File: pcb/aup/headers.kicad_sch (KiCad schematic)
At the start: 4 parts, among them J1 DF40C-100DS-0.4V_51, J2 DF40C-100DS-0.4V_51, J3 DF40C-100DS-0.4V_51, J4 DF40C-100DS-0.4V_51

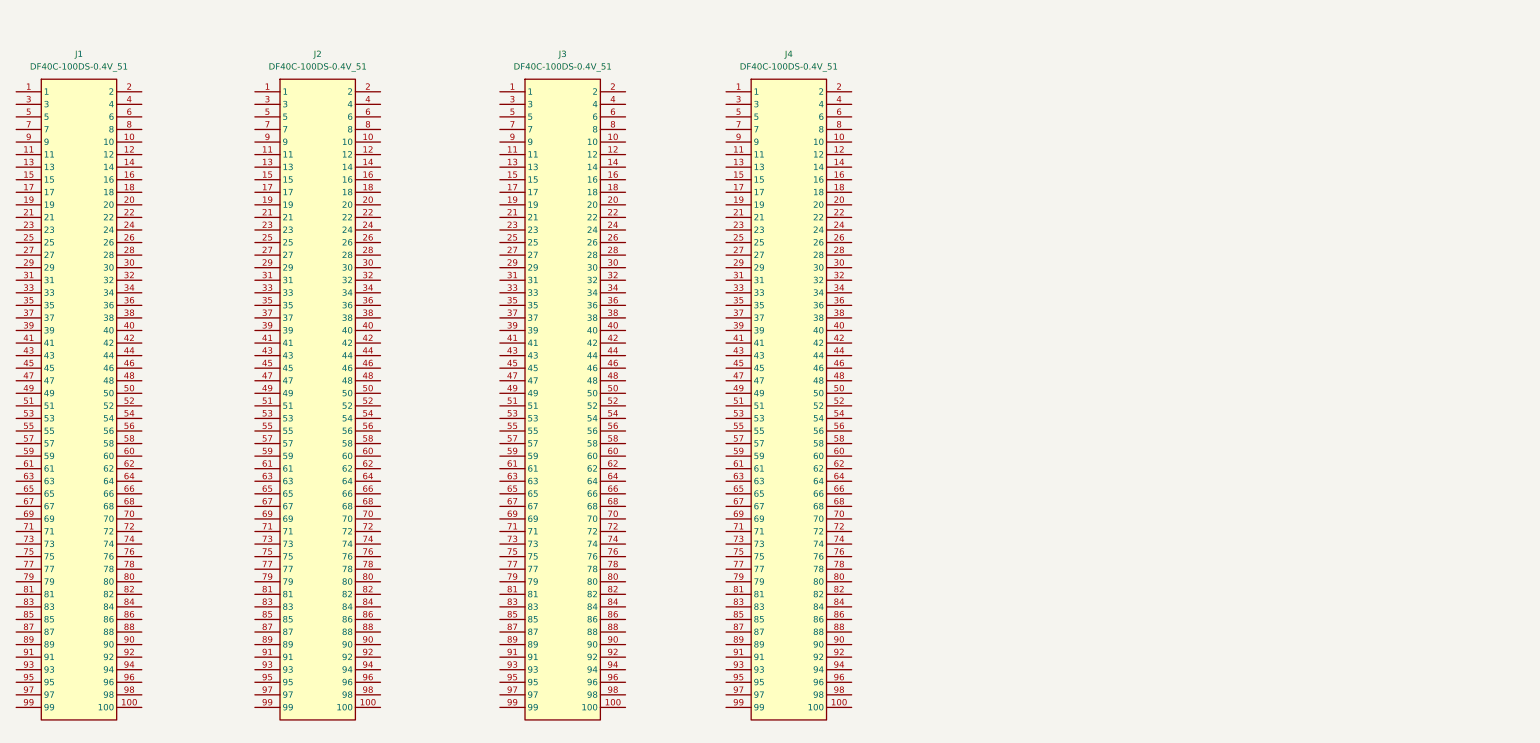
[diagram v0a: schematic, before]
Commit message: Switch to 50 pin sockets
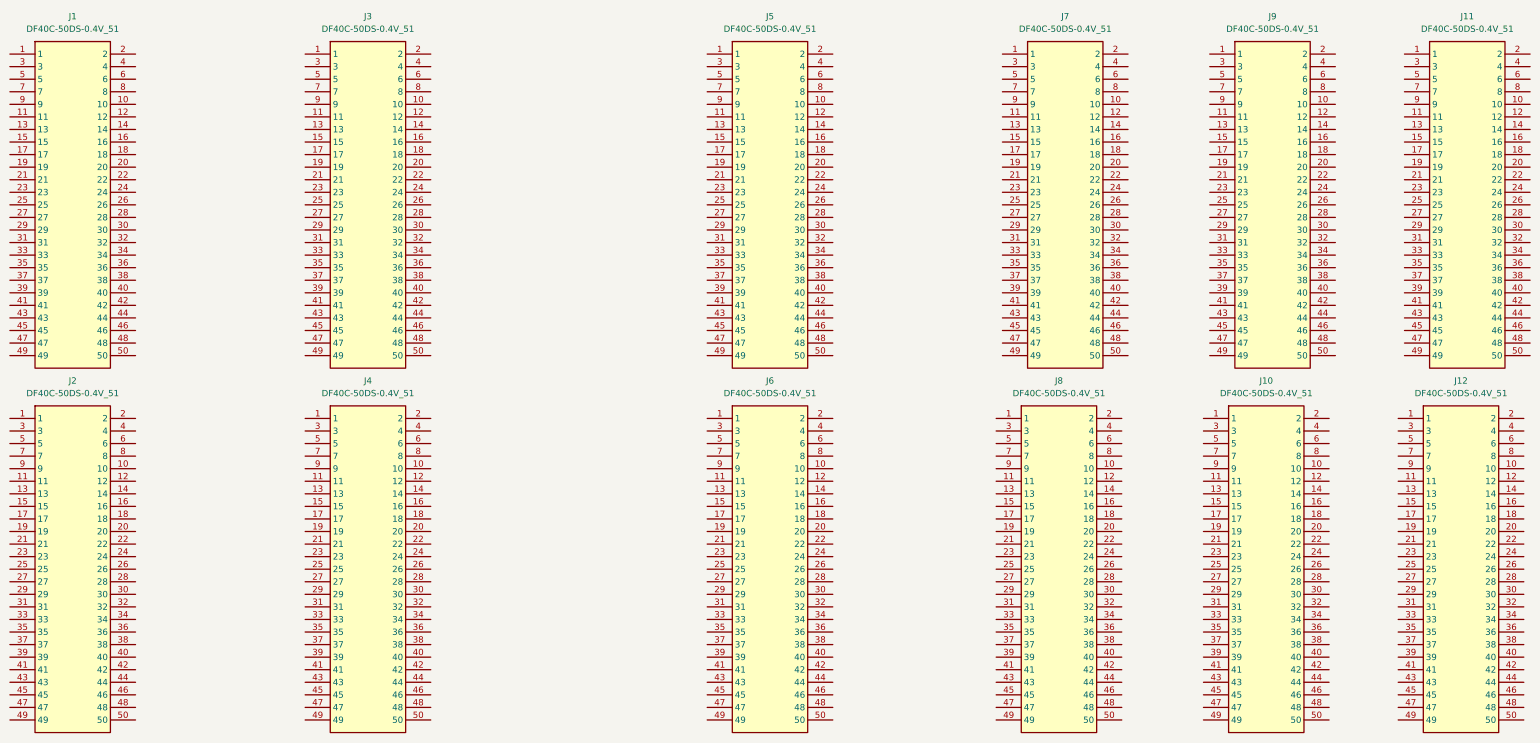
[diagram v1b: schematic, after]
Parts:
- removed J1, J2, J3, J4: DF40C-100DS-0.4V_51, !DF40C:DF40C100DS04V51, symbol !DF40C:DF40C-100DS-0.4V_51
- added J1, J10, J11, J12, J2, J3, J4, J5, J6, J7, J8, J9: DF40C-50DS-0.4V_51, !DF40C:DF40C50DS04VD1, symbol !DF40C:DF40C-50DS-0.4V_51

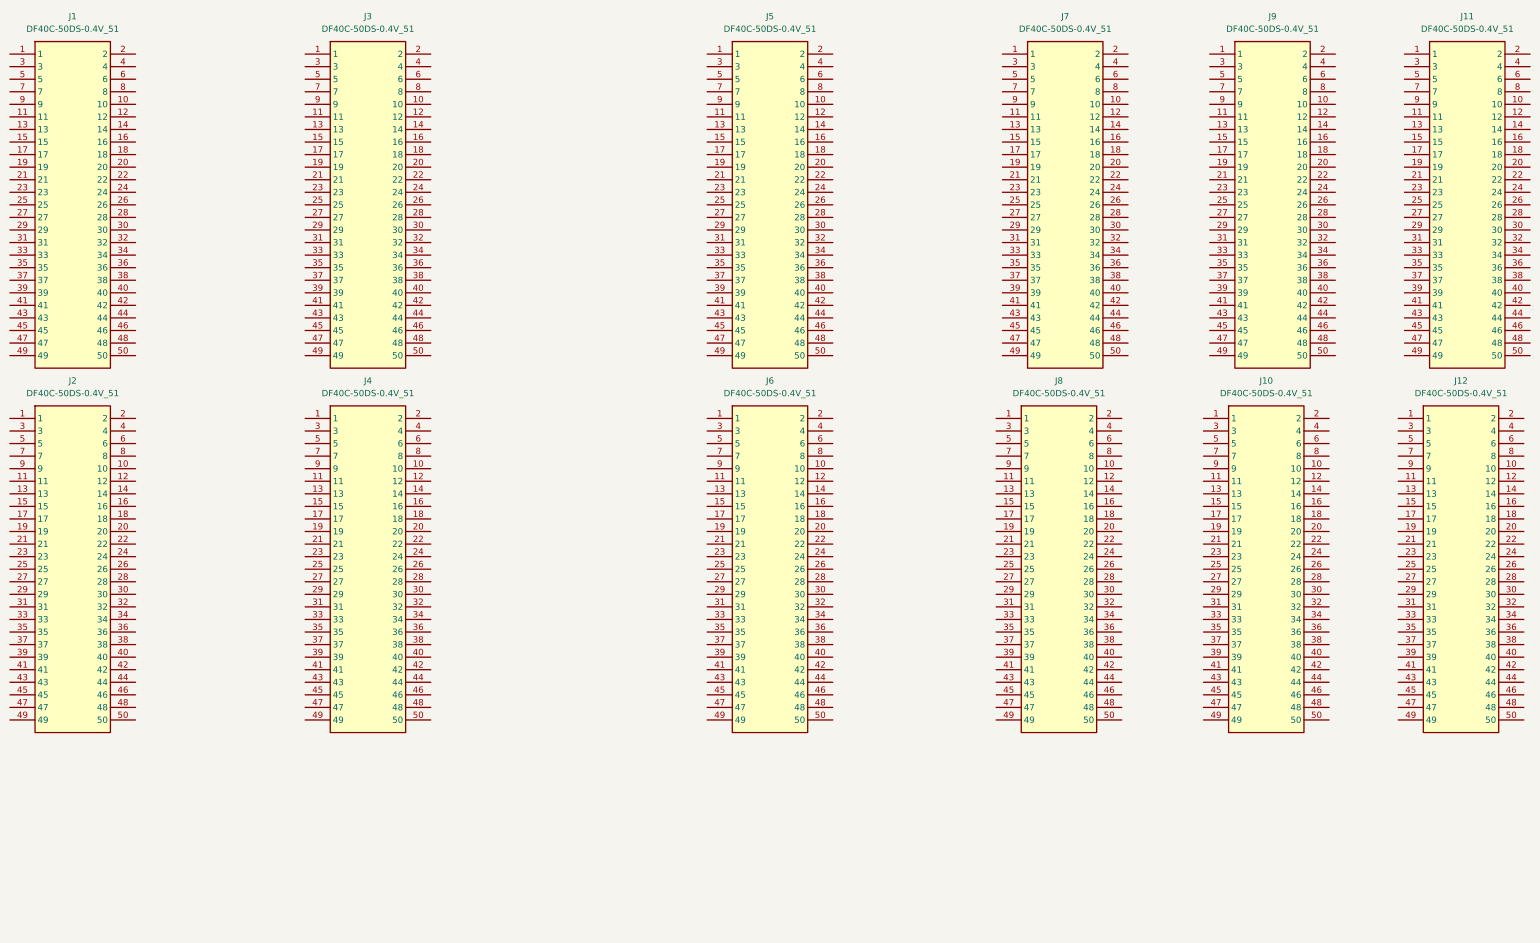
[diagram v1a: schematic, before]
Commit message: Switch to QSH-60
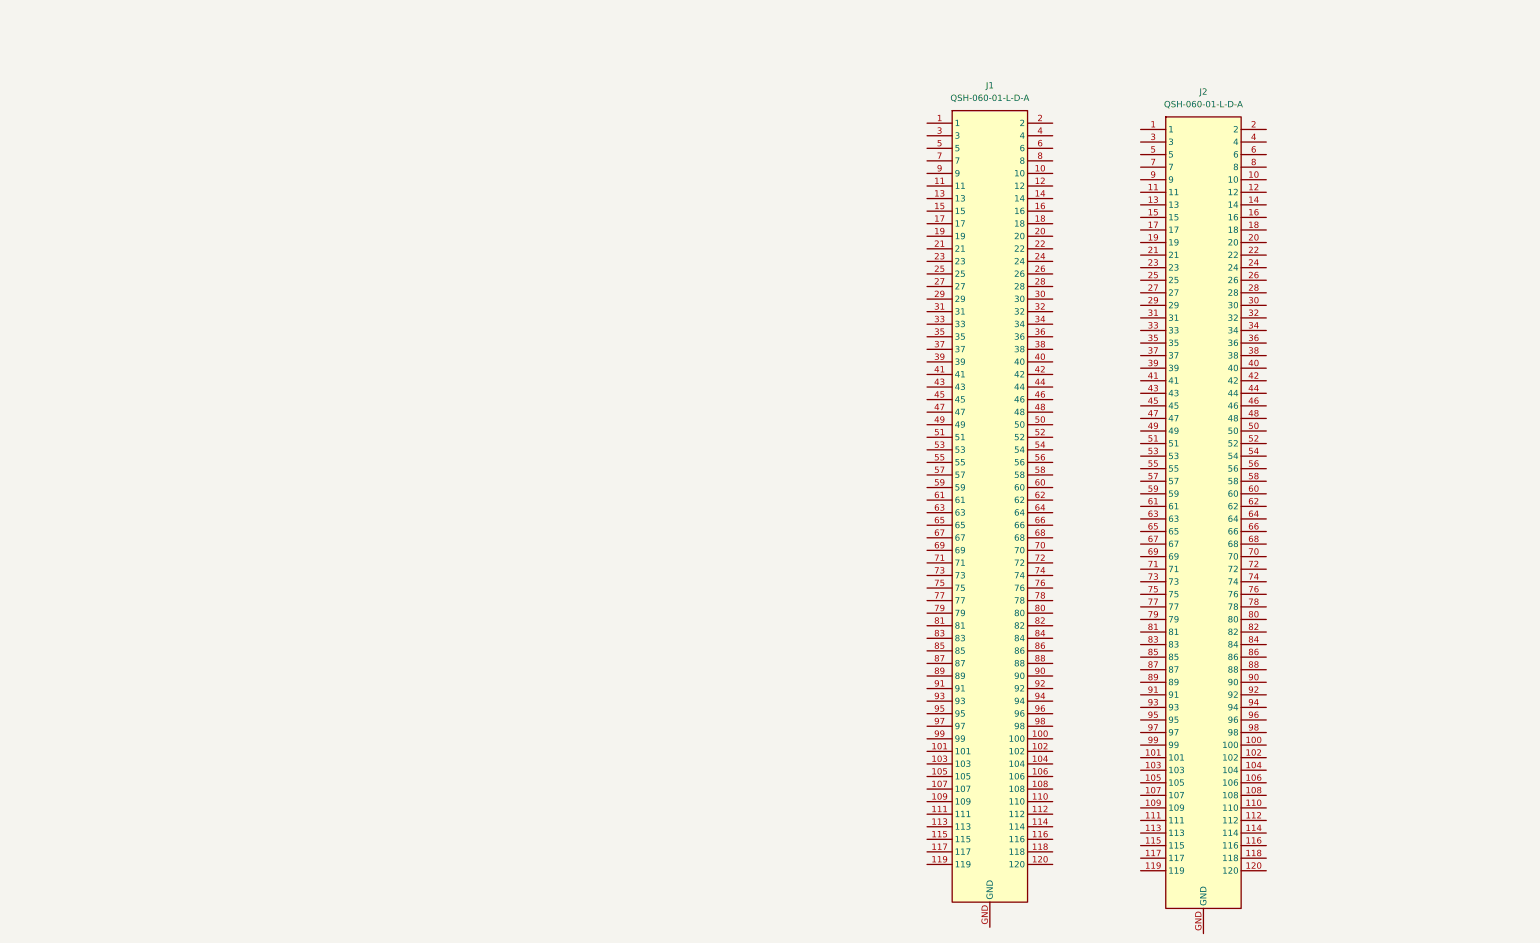
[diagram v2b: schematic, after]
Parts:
- removed J1, J10, J11, J12, J2, J3, J4, J5, J6, J7, J8, J9: DF40C-50DS-0.4V_51, !DF40C:DF40C50DS04VD1, symbol !DF40C:DF40C-50DS-0.4V_51
- added J1, J2: QSH-060-01-L-D-A, !Misc:SAMTEC_QSH-060-01-X-D-A, symbol !Misc:QSH-060-01-L-D-A

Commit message: Add upper connector
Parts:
- added J3, J4: QTH-060-01-L-D-A, !Misc:SAMTEC_QTH-060-01-X-D-A, symbol !Misc:QTH-060-01-L-D-A
- added J5: QSH-030-01-L-D-A, !Misc:SAMTEC_QSH-030-01-X-D-A, symbol !Misc:QSH-030-01-L-D-A
- added J6: QTH-030-01-L-D-A, !Misc:SAMTEC_QTH-030-01-X-D-A, symbol !Misc:QTH-030-01-L-D-A
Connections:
- net IOT_180: now reaches J1.1
- net IOT_180: now also J3.1
- net +3V3: now reaches J1.10
- net +3V3: now also J1.101, J1.102, J1.111, J1.112, J1.19, J1.20, J1.29, J1.30, J1.39, J1.40, J1.49, J1.50, J1.71, J1.72, J1.81, J1.82, J1.9, J1.91, J1.92, J2.10, J2.101, J2.102, J2.111, J2.112, J2.19, J2.20, J2.29, J2.30, J2.39, J2.40, J2.49, J2.50, J2.71, J2.72, J2.81, J2.82, J2.9, J2.91, J2.92, J3.10, J3.101, J3.102, J3.111, J3.112, J3.19, J3.20, J3.29, J3.30, J3.39, J3.40, J3.49, J3.50, J3.71, J3.72, J3.81, J3.82, J3.9, J3.91, J3.92, J4.10, J4.101, J4.102, J4.111, J4.112, J4.19, J4.20, J4.29, J4.30, J4.39, J4.40, J4.49, J4.50, J4.71, J4.72, J4.81, J4.82, J4.9, J4.91, J4.92
- net IOL_17B: now reaches J1.100
- net IOL_17B: now also J3.100
- net IOL_7A: now reaches J1.103
- net IOL_7A: now also J3.103
- net IOL_20B: now reaches J1.104
- net IOL_20B: now also J3.104
- net IOL_21A: now reaches J1.105
- net IOL_21A: now also J3.105
- net IOL_18B: now reaches J1.106
- net IOL_18B: now also J3.106
- net IOL_12A: now reaches J1.107
- net IOL_12A: now also J3.107
- net IOL_21B: now reaches J1.108
- net IOL_21B: now also J3.108
- net IOL_26B: now reaches J1.109
- net IOL_26B: now also J3.109
- net IOT_181: now reaches J1.11
- net IOT_181: now also J3.11
- net IOL_24A: now reaches J1.110
- net IOL_24A: now also J3.110
- net IOL_25B: now reaches J1.113
- net IOL_25B: now also J3.113
- net IOL_25A: now reaches J1.114
- net IOL_25A: now also J3.114
- net IOL_16B: now reaches J1.115
- net IOL_16B: now also J3.115
- net IOL_26A: now reaches J1.116
- net IOL_26A: now also J3.116
- net IOL_22A: now reaches J1.117
- net IOL_22A: now also J3.117
- net IOL_22B: now reaches J1.118
- net IOL_22B: now also J3.118
- net IOL_19B: now reaches J1.119
- net IOL_19B: now also J3.119
- net IOT_182: now reaches J1.12
- net IOT_182: now also J3.12
- net IOL_24B: now reaches J1.120
- net IOL_24B: now also J3.120
- net IOT_185: now reaches J1.13
- net IOT_185: now also J3.13
- net IOT_187: now reaches J1.14
- net IOT_187: now also J3.14
- net IOT_179: now reaches J1.15
- net IOT_179: now also J3.15
- net IOT_169: now reaches J1.16
- net IOT_169: now also J3.16
- net IOT_193: now reaches J1.17
- net IOT_193: now also J3.17
- net IOT_184: now reaches J1.18
- net IOT_184: now also J3.18
- net IOT_176: now reaches J1.2
- net IOT_176: now also J3.2
- net IOT_191: now reaches J1.21
- net IOT_191: now also J3.21
- net IOT_168: now reaches J1.22
- net IOT_168: now also J3.22
- net IOT_192: now reaches J1.23
- net IOT_192: now also J3.23
- net IOT_186: now reaches J1.24
- net IOT_186: now also J3.24
- net IOT_209: now reaches J1.25
- net IOT_209: now also J3.25
- net IOT_183: now reaches J1.26
- net IOT_183: now also J3.26
- net IOT_200: now reaches J1.27
- net IOT_200: now also J3.27
- net IOT_194: now reaches J1.28
- net IOT_194: now also J3.28
- net IOT_196: now reaches J1.3
- net IOT_196: now also J3.3
- net IOT_197: now reaches J1.31
- net IOT_197: now also J3.31
- net IOT_177: now reaches J1.32
- net IOT_177: now also J3.32
- net IOT_219: now reaches J1.33
- net IOT_219: now also J3.33
- net IOT_199: now reaches J1.34
- net IOT_199: now also J3.34
- net IOT_210: now reaches J1.35
- net IOT_210: now also J3.35
- net IOT_203: now reaches J1.36
- net IOT_203: now also J3.36
- net IOT_221: now reaches J1.37
- net IOT_221: now also J3.37
- net IOT_205: now reaches J1.38
- net IOT_205: now also J3.38
- net IOT_171: now reaches J1.4
- net IOT_171: now also J3.4
- net IOT_222: now reaches J1.41
- net IOT_222: now also J3.41
- net IOT_207: now reaches J1.42
- net IOT_207: now also J3.42
- net IOT_206: now reaches J1.43
- net IOT_206: now also J3.43
- net IOT_211: now reaches J1.44
- net IOT_211: now also J3.44
- net IOT_227: now reaches J1.45
- net IOT_227: now also J3.45
- net IOT_208: now reaches J1.46
- net IOT_208: now also J3.46
- net IOT_198: now reaches J1.47
- net IOT_198: now also J3.47
- net IOT_216: now reaches J1.48
- net IOT_216: now also J3.48
- net IOT_190: now reaches J1.5
- net IOT_190: now also J3.5
- net IOT_212: now reaches J1.51
- net IOT_212: now also J3.51
- net IOT_213: now reaches J1.52
- net IOT_213: now also J3.52
- net IOT_224: now reaches J1.53
- net IOT_224: now also J3.53
- net IOT_214: now reaches J1.54
- net IOT_214: now also J3.54
- net IOT_215: now reaches J1.55
- net IOT_215: now also J3.55
- net IOT_223: now reaches J1.56
- net IOT_223: now also J3.56
- net IOT_226: now reaches J1.57
- net IOT_226: now also J3.57
- net IOT_218: now reaches J1.58
- net IOT_218: now also J3.58
- net IOT_225: now reaches J1.59
- net IOT_225: now also J3.59
- net IOT_178: now reaches J1.6
- net IOT_178: now also J3.6
- net IOT_220: now reaches J1.60
- net IOT_220: now also J3.60
- net IOL_2A: now reaches J1.61
- net IOL_2A: now also J3.61
- net IOL_1B: now reaches J1.62
- net IOL_1B: now also J3.62
- net IOL_1A: now reaches J1.63
- net IOL_1A: now also J3.63
- net IOL_2B: now reaches J1.64
- net IOL_2B: now also J3.64
- net IOL_5A: now reaches J1.65
- net IOL_5A: now also J3.65
- net IOL_3B: now reaches J1.66
- net IOL_3B: now also J3.66
- net IOL_6B: now reaches J1.67
- net IOL_6B: now also J3.67
- net IOL_3A: now reaches J1.68
- net IOL_3A: now also J3.68
- net IOL_10A: now reaches J1.69
- net IOL_10A: now also J3.69
- net IOT_173: now reaches J1.7
- net IOT_173: now also J3.7
- net IOL_4B: now reaches J1.70
- net IOL_4B: now also J3.70
- net IOL_19A: now reaches J1.73
- net IOL_19A: now also J3.73
- net IOL_5B: now reaches J1.74
- net IOL_5B: now also J3.74
- net IOL_8B: now reaches J1.75
- net IOL_8B: now also J3.75
- net IOL_10B: now reaches J1.76
- net IOL_10B: now also J3.76
- net IOL_13A: now reaches J1.77
- net IOL_13A: now also J3.77
- net IOL_9B: now reaches J1.78
- net IOL_9B: now also J3.78
- net IOL_4A: now reaches J1.79
- net IOL_4A: now also J3.79
- net IOT_172: now reaches J1.8
- net IOT_172: now also J3.8
- net IOL_13B: now reaches J1.80
- net IOL_13B: now also J3.80
- net IOL_8A: now reaches J1.83
- net IOL_8A: now also J3.83
- net IOL_11B: now reaches J1.84
- net IOL_11B: now also J3.84
- net IOL_20A: now reaches J1.85
- net IOL_20A: now also J3.85
- net IOL_14B: now reaches J1.86
- net IOL_14B: now also J3.86
- net IOL_6A: now reaches J1.87
- net IOL_6A: now also J3.87
- net IOL_12B: now reaches J1.88
- net IOL_12B: now also J3.88
- net IOL_18A: now reaches J1.89
- net IOL_18A: now also J3.89
- net IOL_7B: now reaches J1.90
- net IOL_7B: now also J3.90
- net IOL_23A: now reaches J1.93
- net IOL_23A: now also J3.93
- net IOL_15B: now reaches J1.94
- net IOL_15B: now also J3.94
- net IOL_9A: now reaches J1.95
- net IOL_9A: now also J3.95
- net IOL_15A: now reaches J1.96
- net IOL_15A: now also J3.96
- net IOL_17A: now reaches J1.97
- net IOL_17A: now also J3.97
- net IOL_16A: now reaches J1.98
- net IOL_16A: now also J3.98
- net IOL_11A: now reaches J1.99
- net IOL_11A: now also J3.99
- net GND: now reaches J1.GND
- net GND: now also J2.GND, J3.GND, J4.GND
- net IOR_165: now reaches J2.1
- net IOR_165: now also J4.1
- net IOB_67: now reaches J2.100
- net IOB_67: now also J4.100
- net IOB_75: now reaches J2.103
- net IOB_75: now also J4.103
- net IOB_52: now reaches J2.104
- net IOB_52: now also J4.104
- net IOB_53: now reaches J2.105
- net IOB_53: now also J4.105
- net IOB_82: now reaches J2.106
- net IOB_82: now also J4.106
- net IOB_73: now reaches J2.107
- net IOB_73: now also J4.107
- net IOB_56: now reaches J2.108
- net IOB_56: now also J4.108
- net IOB_71: now reaches J2.109
- net IOB_71: now also J4.109
- net IOR_157: now reaches J2.11
- net IOR_157: now also J4.11
- net IOB_77: now reaches J2.110
- net IOB_77: now also J4.110
- net IOB_69: now reaches J2.113
- net IOB_69: now also J4.113
- net IOB_64: now reaches J2.114
- net IOB_64: now also J4.114
- net IOB_63: now reaches J2.115
- net IOB_63: now also J4.115
- net IOB_54: now reaches J2.116
- net IOB_54: now also J4.116
- net IOB_61: now reaches J2.117
- net IOB_61: now also J4.117
- net IOB_58: now reaches J2.118
- net IOB_58: now also J4.118
- net IOB_57: now reaches J2.119
- net IOB_57: now also J4.119
- net IOR_160: now reaches J2.12
- net IOR_160: now also J4.12
- net IOL_23B: now reaches J2.120
- net IOL_23B: now also J4.120
- net IOR_151: now reaches J2.13
- net IOR_151: now also J4.13
- net IOR_150: now reaches J2.14
- net IOR_150: now also J4.14
- net IOR_147: now reaches J2.15
- net IOR_147: now also J4.15
- net IOR_155: now reaches J2.16
- net IOR_155: now also J4.16
- net IOR_149: now reaches J2.17
- net IOR_149: now also J4.17
- net IOR_146: now reaches J2.18
- net IOR_146: now also J4.18
- net IOR_148: now reaches J2.2
- net IOR_148: now also J4.2
- net IOR_145: now reaches J2.21
- net IOR_145: now also J4.21
- net IOR_144: now reaches J2.22
- net IOR_144: now also J4.22
- net IOR_143: now reaches J2.23
- net IOR_143: now also J4.23
- net IOR_152: now reaches J2.24
- net IOR_152: now also J4.24
- net IOR_130: now reaches J2.25
- net IOR_130: now also J4.25
- net IOR_140: now reaches J2.26
- net IOR_140: now also J4.26
- net IOR_138: now reaches J2.27
- net IOR_138: now also J4.27
- net IOR_142: now reaches J2.28
- net IOR_142: now also J4.28
- net IOR_161: now reaches J2.3
- net IOR_161: now also J4.3
- net IOR_141: now reaches J2.31
- net IOR_141: now also J4.31
- net IOR_139: now reaches J2.32
- net IOR_139: now also J4.32
- net IOR_131: now reaches J2.33
- net IOR_131: now also J4.33
- net IOR_136: now reaches J2.34
- net IOR_136: now also J4.34
- net IOR_133: now reaches J2.35
- net IOR_133: now also J4.35
- net IOR_122: now reaches J2.36
- net IOR_122: now also J4.36
- net IOR_129: now reaches J2.37
- net IOR_129: now also J4.37
- net IOR_126: now reaches J2.38
- net IOR_126: now also J4.38
- net IOR_156: now reaches J2.4
- net IOR_156: now also J4.4
- net IOR_127: now reaches J2.41
- net IOR_127: now also J4.41
- net IOR_116: now reaches J2.42
- net IOR_116: now also J4.42
- net IOR_119: now reaches J2.43
- net IOR_119: now also J4.43
- net IOR_137: now reaches J2.44
- net IOR_137: now also J4.44
- net IOR_121: now reaches J2.45
- net IOR_121: now also J4.45
- net IOR_114: now reaches J2.46
- net IOR_114: now also J4.46
- net IOR_109: now reaches J2.47
- net IOR_109: now also J4.47
- net IOR_134: now reaches J2.48
- net IOR_134: now also J4.48
- net IOR_167: now reaches J2.5
- net IOR_167: now also J4.5
- net IOR_123: now reaches J2.51
- net IOR_123: now also J4.51
- net IOR_120: now reaches J2.52
- net IOR_120: now also J4.52
- net IOR_117: now reaches J2.53
- net IOR_117: now also J4.53
- net IOR_115: now reaches J2.54
- net IOR_115: now also J4.54
- net IOR_112: now reaches J2.55
- net IOR_112: now also J4.55
- net IOR_128: now reaches J2.56
- net IOR_128: now also J4.56
- net IOR_113: now reaches J2.57
- net IOR_113: now also J4.57
- net IOR_111: now reaches J2.58
- net IOR_111: now also J4.58
- net IOR_110: now reaches J2.59
- net IOR_110: now also J4.59
- net IOR_154: now reaches J2.6
- net IOR_154: now also J4.6
- net IOR_118: now reaches J2.60
- net IOR_118: now also J4.60
- net IOB_102: now reaches J2.61
- net IOB_102: now also J4.61
- net IOB_101: now reaches J2.62
- net IOB_101: now also J4.62
- net IOB_100: now reaches J2.63
- net IOB_100: now also J4.63
- net IOB_98: now reaches J2.64
- net IOB_98: now also J4.64
- net IOB_91: now reaches J2.65
- net IOB_91: now also J4.65
- net IOB_93: now reaches J2.66
- net IOB_93: now also J4.66
- net IOB_92: now reaches J2.67
- net IOB_92: now also J4.67
- net IOB_105_SDO: now reaches J2.68
- net IOB_105_SDO: now also J4.68
- net IOB_103_CBSEL1: now reaches J2.69
- net IOB_103_CBSEL1: now also J4.69
- net IOR_153: now reaches J2.7
- net IOR_153: now also J4.7
- net IOB_106_SDI: now reaches J2.70
- net IOB_106_SDI: now also J4.70
- net IOB_60: now reaches J2.73
- net IOB_60: now also J4.73
- net IOB_87: now reaches J2.74
- net IOB_87: now also J4.74
- net IOB_94: now reaches J2.75
- net IOB_94: now also J4.75
- net IOB_86: now reaches J2.76
- net IOB_86: now also J4.76
- net IOB_107_SCK: now reaches J2.77
- net IOB_107_SCK: now also J4.77
- net IOB_99: now reaches J2.78
- net IOB_99: now also J4.78
- net IOB_89: now reaches J2.79
- net IOB_89: now also J4.79
- net IOR_162: now reaches J2.8
- net IOR_162: now also J4.8
- net IOB_85: now reaches J2.80
- net IOB_85: now also J4.80
- net IOB_84: now reaches J2.83
- net IOB_84: now also J4.83
- net IOB_74: now reaches J2.84
- net IOB_74: now also J4.84
- net IOB_88: now reaches J2.85
- net IOB_88: now also J4.85
- net IOB_78: now reaches J2.86
- net IOB_78: now also J4.86
- net IOB_81: now reaches J2.87
- net IOB_81: now also J4.87
- net IOB_72: now reaches J2.88
- net IOB_72: now also J4.88
- net IOB_59: now reaches J2.89
- net IOB_59: now also J4.89
- net IOB_80: now reaches J2.90
- net IOB_80: now also J4.90
- net IOB_79: now reaches J2.93
- net IOB_79: now also J4.93
- net IOB_103_CBSEL0: now reaches J2.94
- net IOB_103_CBSEL0: now also J4.94
- net IOB_83: now reaches J2.95
- net IOB_83: now also J4.95
- net IOB_66: now reaches J2.96
- net IOB_66: now also J4.96
- net IOB_76: now reaches J2.97
- net IOB_76: now also J4.97
- net IOB_68: now reaches J2.98
- net IOB_68: now also J4.98
- net IOB_55: now reaches J2.99
- net IOB_55: now also J4.99
